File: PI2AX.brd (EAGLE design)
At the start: 15.2 x 16.5 mm, 5 parts, among them IC1 SN74LVC2G241

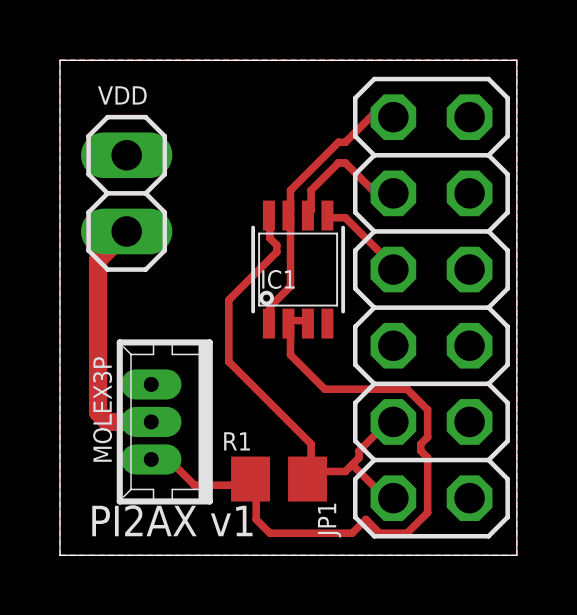
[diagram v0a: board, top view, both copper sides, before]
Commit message: revised v1.1, molex connector fixed
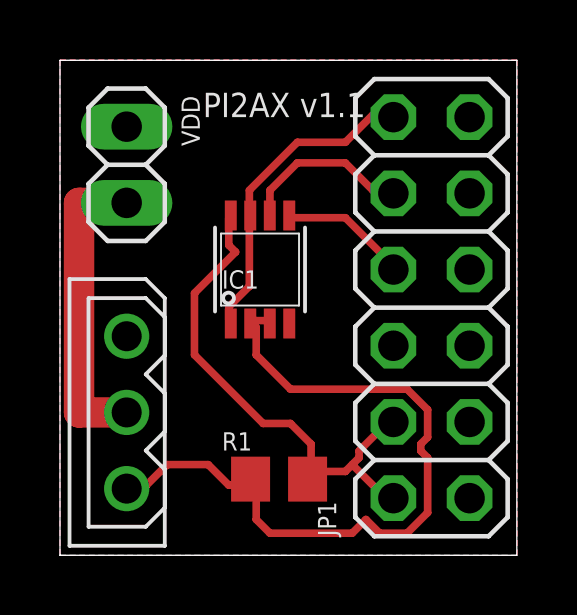
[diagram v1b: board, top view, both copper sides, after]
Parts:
- removed MOLEX3P: MOLEX3P, con-molex:53047-03
- added J1: 22-03-5035, molex:5267-3
- moved IC1 1.27 mm to (6.99, 10.2)
- moved VDD 0.95 mm to (2.54, 13.7)
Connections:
- net GND: now also J1.1; no longer MOLEX3P.1
- net OUTPUT: now also J1.3; no longer MOLEX3P.3
- net VDD: now also J1.2; no longer MOLEX3P.2
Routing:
- net OUTPUT: track 22.6 -> 24.9 mm
- net VDD: track 8.33 -> 10.2 mm
- net DIR-PIN: track 9.32 -> 10.7 mm
- net RX: track 4.48 -> 5.82 mm
- net TX: track 3.01 -> 4.30 mm
- net VCC: track 16.6 -> 17.5 mm
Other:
- board text added: "PI2AX v1.1"
- board text removed: "PI2AX v1"
